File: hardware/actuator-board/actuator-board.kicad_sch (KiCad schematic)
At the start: 0 parts

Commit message: Harware designs, and log analysis
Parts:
- added C1, C3: 100nF, symbol Device:C
- added C2, C4: 10uF, symbol Device:C
- added D1: SS34, Diode_SMD:D_SMA, symbol Diode:SS34
- added D2, D3: US1J, Diode_SMD:D_SMA, symbol Diode:US1J
- added D4: LED, symbol Device:LED
- added J1: RudderSense, symbol Connector:Conn_01x03_Pin
- added J2: HBridge, symbol Connector:Conn_01x03_Pin
- added J4: UDPI, symbol Connector:Conn_01x01_Pin
- added J5: Clutch, symbol Connector:Screw_Terminal_01x02
- added J6: HBridgeSupply, symbol Connector:Screw_Terminal_01x02
- added J7: SerialToPi, symbol Connector:Conn_01x03_Pin
- added Q1: IRF540N, Package_TO_SOT_THT:TO-220-3_Vertical, symbol Transistor_FET:IRF540N
- added R1: 470R, symbol Device:R
- added R2: 100R, symbol Device:R
- added R3: R_Shunt, symbol Device:R_Shunt
- added R4: 1K, symbol Device:R
- added U1: INA219AxD, Package_SO:SOIC-8_3.9x4.9mm_P1.27mm, symbol Sensor_Energy:INA219AxD
- added U2: ATtiny3224-SS, Package_SO:SOIC-14_3.9x8.7mm_P1.27mm, symbol MCU_Microchip_ATtiny:ATtiny3224-SS
- added U3: AMS1117-3.3, Package_TO_SOT_SMD:SOT-223-3_TabPin2, symbol Regulator_Linear:AMS1117-3.3
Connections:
- new net: Q1.1 (G), R2.2
- new net: R3.2, U1.7 (IN-)
- new net: R3.3, U1.8 (IN+)
- new net: D4.1 (K), R4.2
- new net: D4.2 (A), U2.13 (PA3)
- new net: D1.2 (A), J5.2 (Pin_2), Q1.2 (D)
- new net: J6.2 (Pin_2), R3.1
- new net: J4.1 (Pin_1), R1.2
- new net +12V: C4.1, D1.1 (K), J5.1 (Pin_1), J6.1 (Pin_1), R3.4, U3.3 (VI)
- new net +3V3: C1.1, C2.1, C3.1, D2.1 (K), J1.1 (Pin_1), U1.5 (VS), U2.1 (VCC), U3.2 (VO)
- new net Clutch: R2.1, U2.4 (PA6)
- new net GND: C1.2, C2.2, C3.2, C4.2, D3.2 (A), J1.3 (Pin_3), J2.3 (Pin_3), J7.1 (Pin_1), Q1.3 (S), R4.1, U1.6 (GND), U2.14 (GND), U3.1 (GND)
- new net PWMPort: J2.1 (Pin_1), U2.2 (PA4)
- new net PWMStbd: J2.2 (Pin_2), U2.3 (PA5)
- new net RX: J7.2 (Pin_2), U2.6 (PB3)
- new net Rudder: D2.2 (A), D3.1 (K), J1.2 (Pin_2), U2.11 (PA1)
- new net SCL: U1.4 (SCL), U2.9 (PB0)
- new net SDA: U1.3 (SDA), U2.8 (PB1)
- new net TX: J7.3 (Pin_3), U2.7 (PB2)
- new net UDPI: R1.1, U2.10 (~{RESET}/PA0)
- no-connect marks 0 -> 2
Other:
- note removed: "--- CLUTCH DRIVER ---"
- note removed: "--- CONNECTORS ---"
- note removed: "--- CURRENT SENSING (OPTION A: Discrete) ---"
- note removed: "--- CURRENT SENSING (OPTION B: INA219) ---"
- note removed: "--- H-BRIDGE INTERFACE ---"
- note removed: "--- MCU: ATtiny3226 ---"
- note removed: "--- POWER SUPPLY ---"
- note removed: "--- VOLTAGE SENSING ---"
- note removed: "12V Input → AP2112K-3.3 LDO → 3.3V Rail Components: U2 - AP2112K-3.3 (SOT-23-5) C1 - 10uF ceramic (input) C2 - 10uF ceramic (output) C3 - 100nF ceramic (MCU decoupling)"
- note removed: "=== BILL OF MATERIALS === MCU: U1 - ATtiny3226-SU (SOIC-20) Power: U2 - AP2112K-3.3 (SOT-23-5) C1,C2 - 10uF 25V X5R 0805 C3 - 100nF 16V X7R 0603 Current Sensing (Option A): R_SHUNT - 0.002Ω 1% 5W (Vishay WSL2512) U3 - MCP6002-I/SN (SOIC-8) R1,R3,R4 - 10kΩ 1% 0603 R2 - 500kΩ 1% 0603 C4 - 100pF 0603 (optional) Current Sensing (Option B - Recommended): U3 - INA219BIDCNR (VSSOP-8) or module R_SHUNT -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"
- note removed: "=== CURRENT SENSING OPTIONS === OPTION A: Discrete Shunt + Op-Amp (shown) Pros: - Lower cost ($0.50 vs $3-5) - No I2C overhead - Faster sampling (direct ADC) Cons: - Requires careful layout - Temperature drift - Gain calibration needed - Ground offset issues OPTION B: INA219/INA226 I2C Module Pros: - Integrated calibration - High accuracy (1%) - Temperature compensated - Reports current + voltage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"
- note removed: "ACTUATOR CONTROLLER SCHEMATIC This schematic shows the current sensing circuit in detail. Consider using INA219/INA226 I2C module as alternative. See notes below for trade-off analysis."
- note removed: "Connection to BTS7960 H-Bridge Module: J2 - 6-pin connector ┌────────────────────┐ │ 1 GND │ │ 2 VCC (5V from HB)│ (optional, for level shift) │ 3 R_EN (enable) │ ← tie to VCC or use GPIO │ 4 L_EN (enable) │ ← tie to VCC or use GPIO │ 5 RPWM (stbd) │ ← PA5 (3.3V logic OK) │ 6 LPWM (port) │ ← PA4 (3.3V logic OK) └────────────────────┘ BTS7960 accepts 3.3V logic on PWM inputs. Enable pins can be ti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"
- note removed: "Differential Amplifier Circuit: R3 = 10k ┌────/\/\/\────┐ │ │ V_shunt+│ ┌─────┐ │ ────────┼────┤- │ │ │ │ U3A ├───┴──── V_out (to PA2) │ ┌──┤+ │ │ │ └─────┘ V_shunt-│ │ ────────┼─┤ R1 = 10k R2 = 500k │ └────/\/\/\────┬────/\/\/\──── GND │ │ └────/\/\/\──────┘ R4 = 10k Gain = R2/R1 = 500k/10k = 50 Components: R_SHUNT - 0.002Ω 1% 5W (Vishay WSL2512) U3 - MCP6002-I/SN (dual rail-to-rail op-amp) R1,R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"
- note removed: "INA219 I2C Current/Voltage Monitor: 12V ────┬──────────────────┬──── Motor+ │ │ │ ┌─────────┐ │ └────┤VIN+ ├───┘ │ INA219 │ ┌────┤VIN- │ │ │ │ Motor- ┴ │ SDA ────┼──── PA2 (I2C) │ SCL ────┼──── PA3 (I2C) │ GND ────┼──── GND │ VCC ────┼──── 3.3V │ A0,A1 ──┼──── GND (addr 0x40) └─────────┘ Internal 0.1Ω shunt (or external for higher current) For 15A max, use external 0.01Ω shunt: - INA219 set to 16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"
- note removed: "J1 - Serial to Pi (JST-SH 4-pin) 1. GND 2. TX (to Pi RX) 3. RX (from Pi TX) 4. VCC (5V from Pi, optional) J2 - H-Bridge (JST-XH 6-pin) See above J3 - Clutch (JST-XH 2-pin) 1. Clutch+ 2. Clutch- (switched to GND) J4 - Rudder Pot (JST-XH 3-pin) 1. VCC (3.3V) 2. Wiper (to PA1) 3. GND J5 - Power (screw terminal 2-pin) 1. 12V 2. GND J6 - UPDI Programming (1x3 header 2.54mm) 1. UPDI (PA0) 2. VCC 3. GND"
- note removed: "Low-Side Shunt Configuration: Motor- ────┬──── GND │ ┌─┴─┐ │R_s│ R_SHUNT = 0.005Ω 1% 3W └─┬─┘ │ ┌───────────┴───────────┐ │ V_shunt │ │ (I × 0.005 = mV) │ └───────────────────────┘ │ ┌──────┴──────┐ │ Diff Amp │ │ Gain = 100 │ U3 - MCP6002 or similar └──────┬──────┘ │ V_out = I × 0.5V/A │ To PA2 (ADC) At 15A: V_out = 15 × 0.5 = 7.5V (needs clamping!) At 12A: V_out = 12 × 0.5 = 6.0V (still too hig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"
- note removed: "N-FET Low-Side Switch with Flyback Protection: 12V ────┬──────────────────────┬──── Clutch+ │ │ │ ┌──────────────┐ │ │ │ Clutch │ │ │ │ Coil │──┘ │ │ (~1A) │ │ └──────┬───────┘ │ │ D2 ─┴─ ◄────────┤ D2 = SS34 Schottky │ │ (flyback diode) │ │ │ ┌───┴───┐ │ │ D │ │ │ │ Q1 = IRLML6344 PA6 ────┼── R7 ─┤ G │ (N-FET, 30V, 5A) │ │ │ │ │ S │ │ └───┬───┘ │ │ GND ────┴───────────┴────────── R7 = 100Ω (gate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"
- note removed: "Resistor Divider for 12V Monitoring: 12V ────┬──── R5 = 30kΩ ────┬──── PA3 (ADC) │ │ │ ─┴─ C5 = 100nF │ ─┬─ │ │ └──── R6 = 10kΩ ────┴──── GND V_out = 12V × 10k/(30k+10k) = 3.0V ✓ V_out = 14V × 10k/(30k+10k) = 3.5V (slightly over 3.3V) Add Zener clamp: D1 - 3.3V Zener across C5 for overvoltage protection"
- note removed: "U1 - ATtiny3226-SU (SOIC-20) Pin Assignment: PA0 - UPDI (programming) PA1 - ADC1 (Rudder potentiometer) PA2 - ADC2 (Current sense) OR I2C SDA PA3 - ADC3 (Voltage sense) OR I2C SCL PA4 - PWM_PORT (TCA0 WO4) PA5 - PWM_STBD (TCA0 WO5) PA6 - CLUTCH (N-FET gate) PA7 - LED (status) PB2 - TX (to Pi RX) PB3 - RX (from Pi TX) VDD - 3.3V GND - Ground"

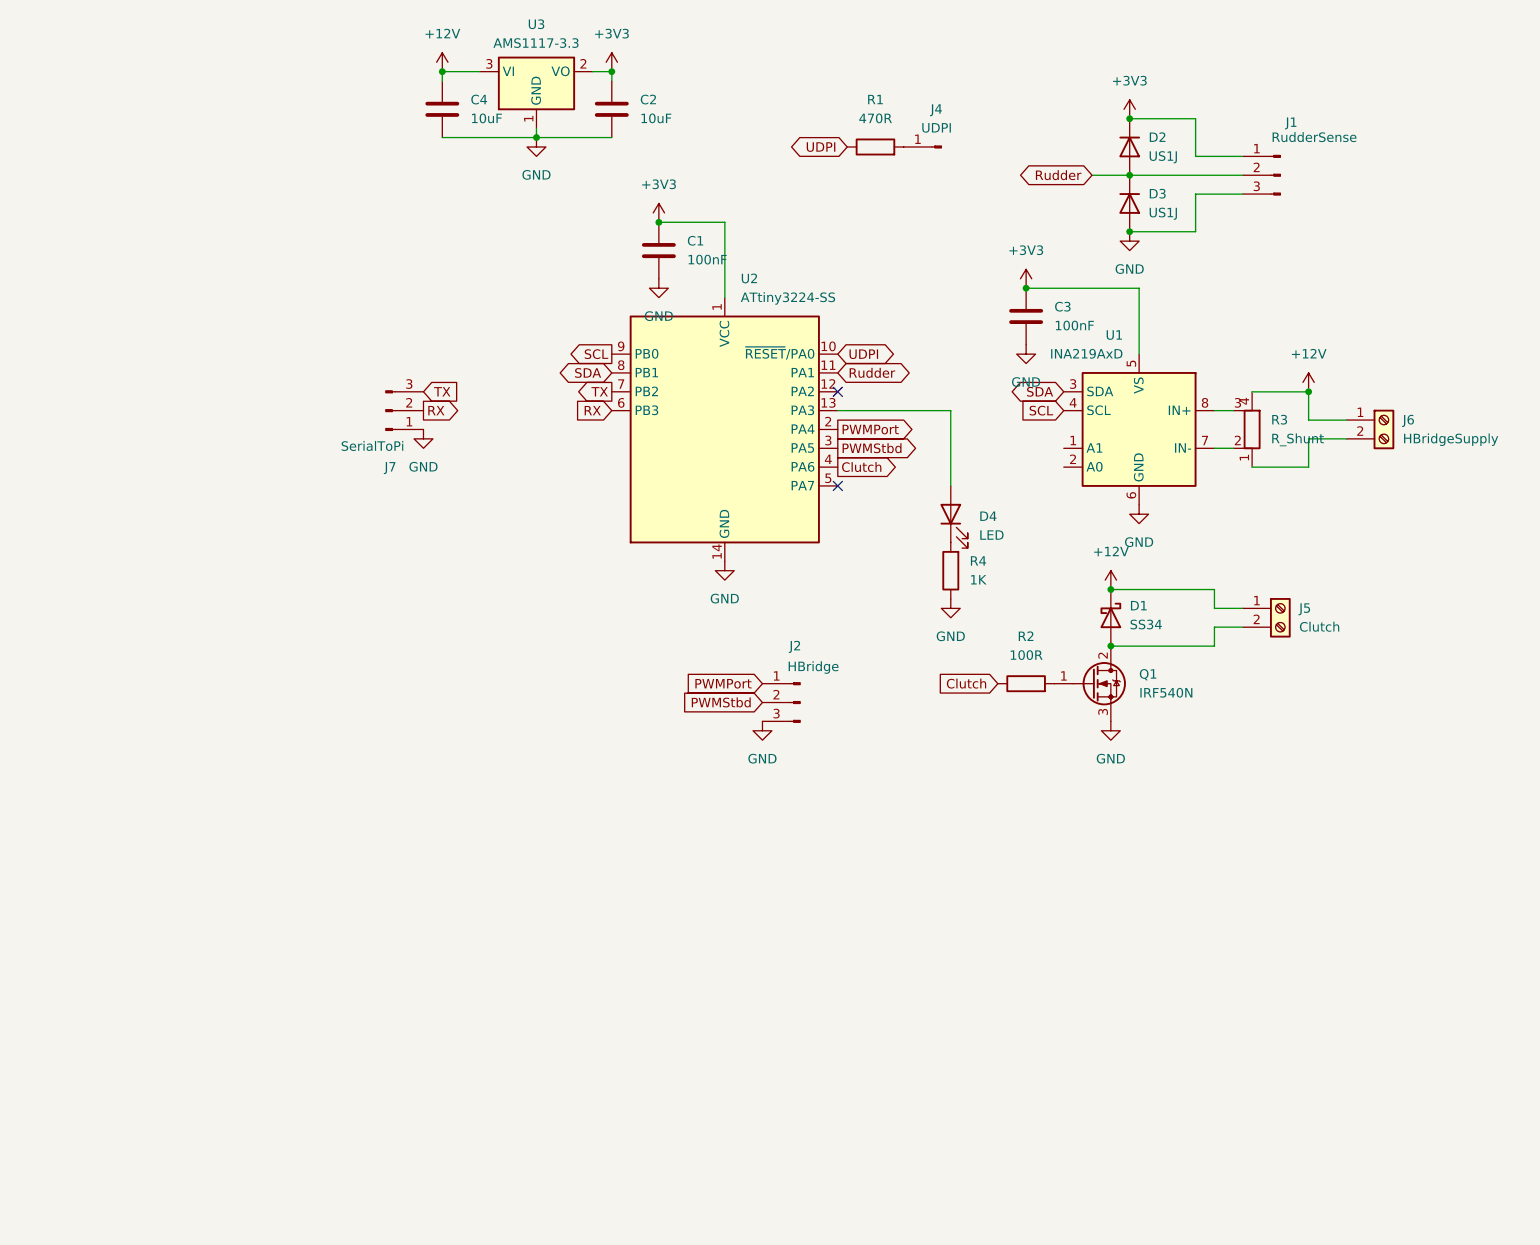
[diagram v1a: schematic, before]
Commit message: Added hardware design for actuator board
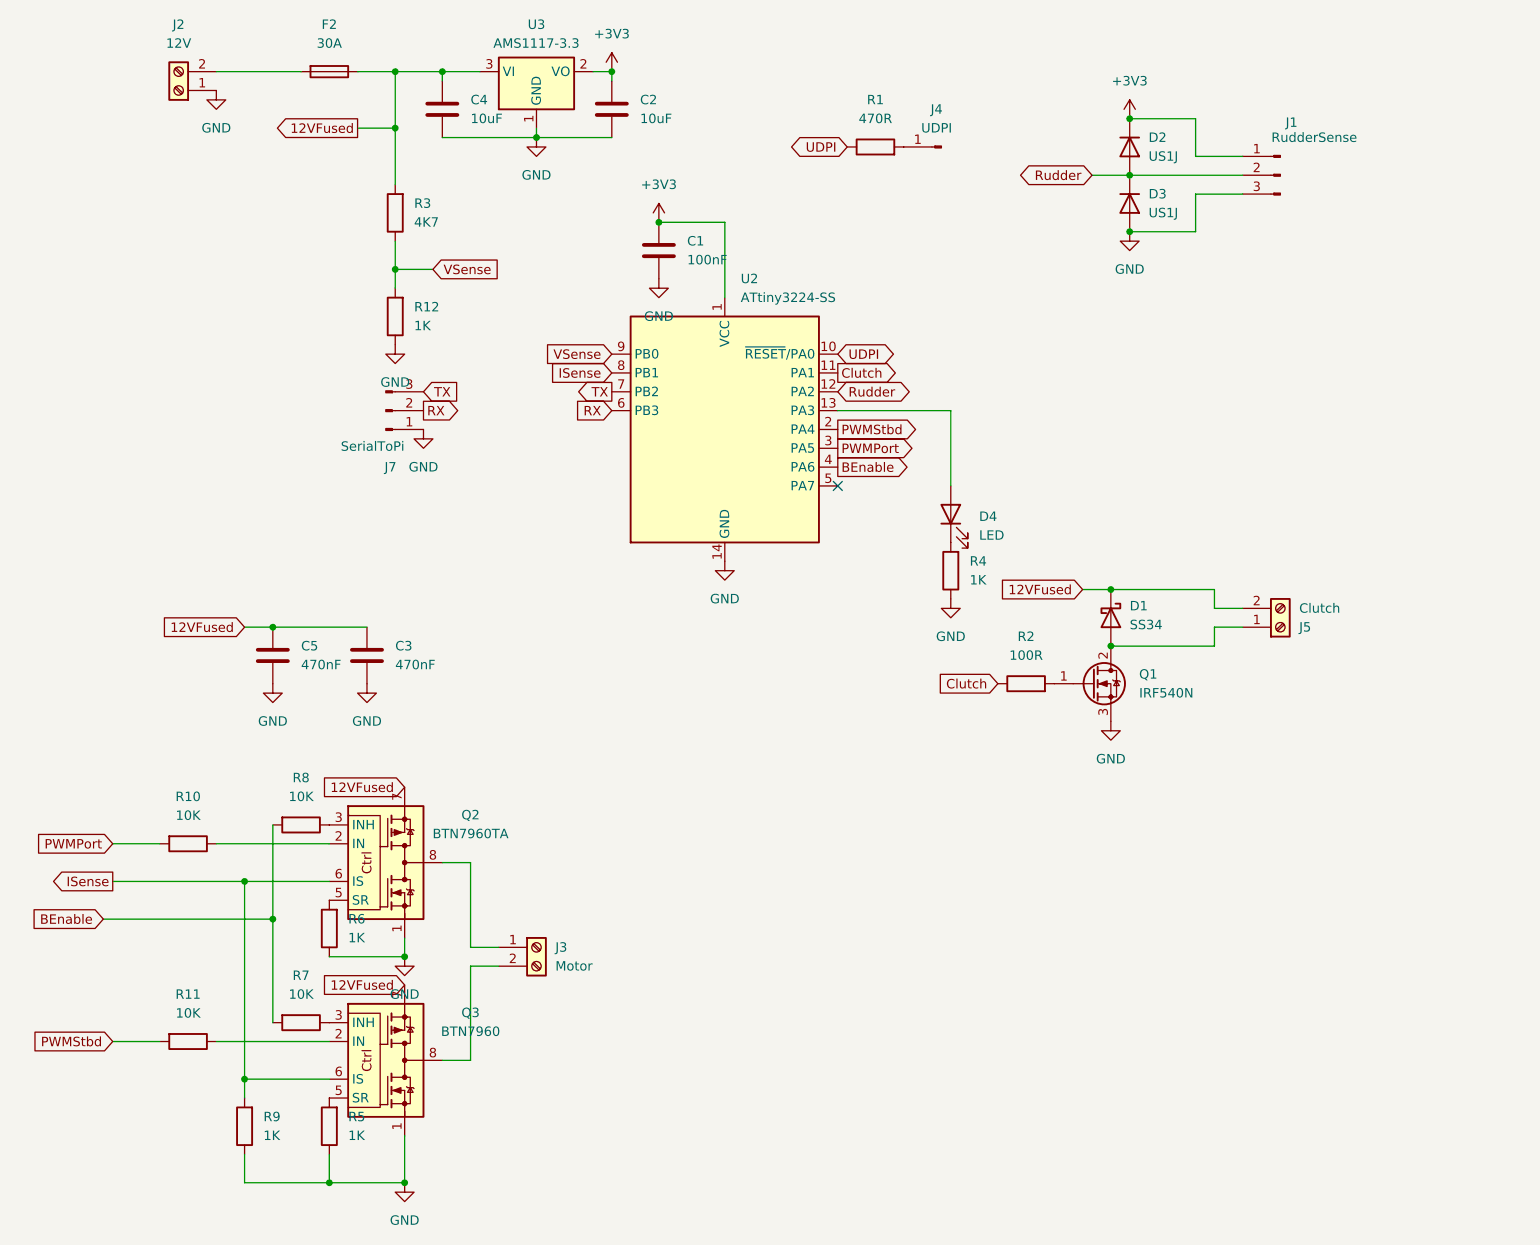
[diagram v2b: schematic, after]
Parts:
- removed J2: HBridge, symbol Connector:Conn_01x03_Pin
- removed J6: HBridgeSupply, symbol Connector:Screw_Terminal_01x02
- removed R3: R_Shunt, symbol Device:R_Shunt
- removed U1: INA219AxD, Package_SO:SOIC-8_3.9x4.9mm_P1.27mm, symbol Sensor_Energy:INA219AxD
- added C5: 470nF, Capacitor_SMD:C_0805_2012Metric, symbol Device:C
- added F2: 30A, Fuse:Fuse_Blade_ATO_directSolder, symbol Device:Fuse
- added J2: 12V, TerminalBlock_Phoenix:TerminalBlock_Phoenix_MKDS-1,5-2-5.08_1x02_P5.08mm_Horizontal, symbol Connector:Screw_Terminal_01x02
- added J3: Motor, TerminalBlock_Phoenix:TerminalBlock_Phoenix_MKDS-1,5-2-5.08_1x02_P5.08mm_Horizontal, symbol Connector:Screw_Terminal_01x02
- added Q2: BTN7960TA, Package_TO_SOT_SMD:TO-263-7_TabPin8, symbol Power_Management:BTN8982TA
- added Q3: BTN7960, Package_TO_SOT_SMD:TO-263-7_TabPin8, symbol Power_Management:BTN8982TA
- added R10, R11, R7, R8: 10K, Resistor_SMD:R_0805_2012Metric, symbol Device:R
- added R12, R5, R6, R9: 1K, Resistor_SMD:R_0805_2012Metric, symbol Device:R
- added R3: 4K7, Resistor_SMD:R_0805_2012Metric, symbol Device:R
- C1, C2, C4, D4: footprint (none) -> Capacitor_SMD:C_0805_2012Metric
- C3: value 100nF -> 470nF; footprint (none) -> Capacitor_SMD:C_0805_2012Metric
- J1: footprint (none) -> TerminalBlock_Phoenix:TerminalBlock_Phoenix_MPT-0,5-3-2.54_1x03_P2.54mm_Horizontal
- J4: footprint (none) -> Connector_PinHeader_1.00mm:PinHeader_1x01_P1.00mm_Vertical
- J5: footprint (none) -> TerminalBlock_Phoenix:TerminalBlock_Phoenix_MPT-0,5-2-2.54_1x02_P2.54mm_Horizontal
- J7: footprint (none) -> Connector_JST:JST_XH_B3B-XH-AM_1x03_P2.50mm_Vertical
- R1, R2, R4: footprint (none) -> Resistor_SMD:R_0805_2012Metric
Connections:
- net +3V3: no longer C3.1
- net Clutch: now also U2.11 (PA1); no longer U2.4 (PA6)
- net GND: now also C5.2, J2.1 (Pin_1), Q2.1, Q3.1, R12.1, R5.1, R6.1, R9.1
- net PWMPort: now also U2.3 (PA5), R10.2; no longer U2.2 (PA4)
- net PWMStbd: now also U2.2 (PA4), R11.2; no longer U2.3 (PA5)
- net Rudder: now also U2.12 (PA2); no longer U2.11 (PA1)
- net at D1.2 (A), Q1.2 (D): now also J5.1 (Pin_1); no longer J5.2 (Pin_2)
- net +12V renamed 12VFused
- net 12VFused: now also C3.1, J5.2 (Pin_2), C5.1, F2.1, Q2.7, Q3.7, R3.2; no longer J5.1 (Pin_1)
- net SCL renamed VSense
- net VSense: now also R12.2, R3.1
- net SDA renamed ISense
- net ISense: now also Q2.6 (IS), Q3.6 (IS), R9.2
- new net: Q3.5 (SR), R5.2
- new net: Q3.2 (IN), R11.1
- new net: F2.2, J2.2 (Pin_2)
- new net: Q3.3 (INH), R7.1
- new net: J3.2 (Pin_2), Q3.4, Q3.8
- new net: Q2.5 (SR), R6.2
- new net: Q2.3 (INH), R8.1
- new net: Q2.2 (IN), R10.1
- new net: J3.1 (Pin_1), Q2.4, Q2.8
- new net BEnable: R7.2, R8.2, U2.4 (PA6)
- no-connect marks 2 -> 1
